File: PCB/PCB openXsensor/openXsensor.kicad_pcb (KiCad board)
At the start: 2 copper layers, 35.6 x 34.3 mm, 18 parts, among them P1 Digital, P10 VFAS/COURANT, P11 GY-86, P12 NTC1, P13 NTC2, P14 ISP1, P15 ISP2, P16 4S, P17 ADS1115, P2 Analog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

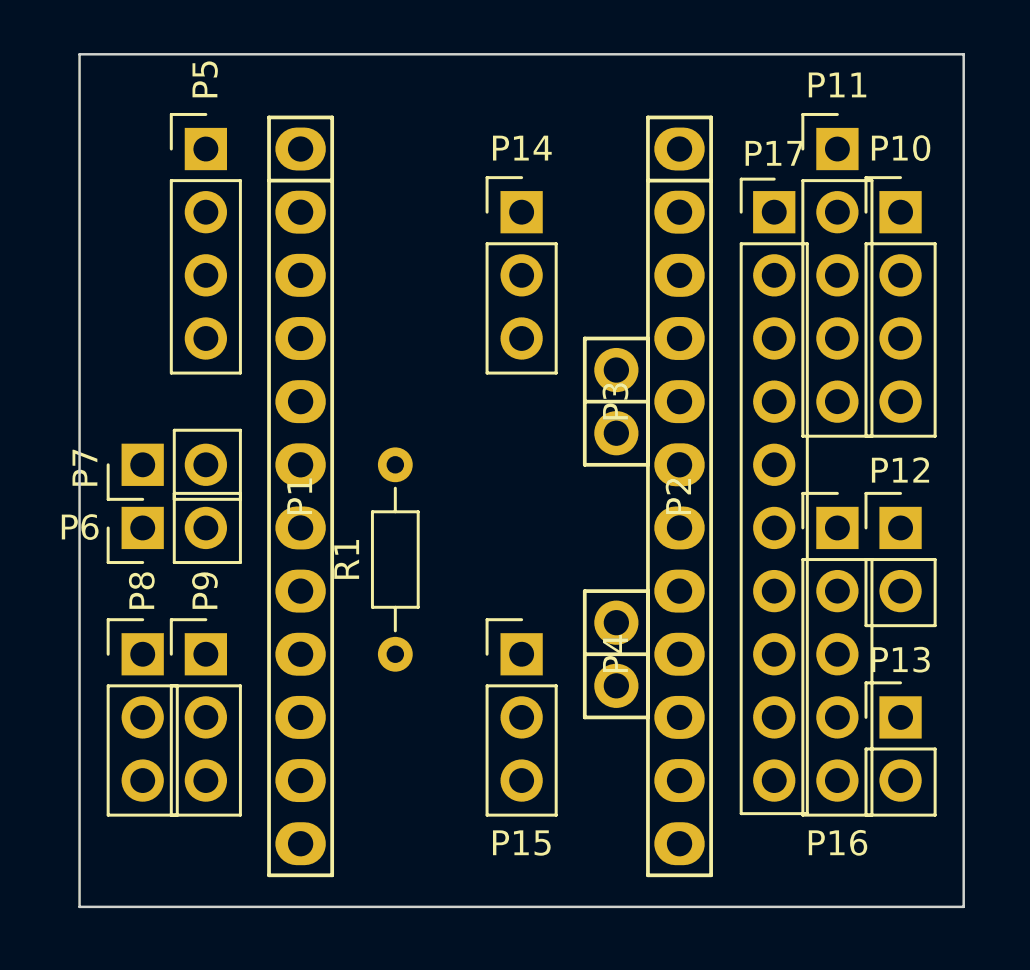
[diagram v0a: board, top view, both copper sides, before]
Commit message: Update oXs pcb proto
Add protection resistors for 4s ans sport/hub connectors.
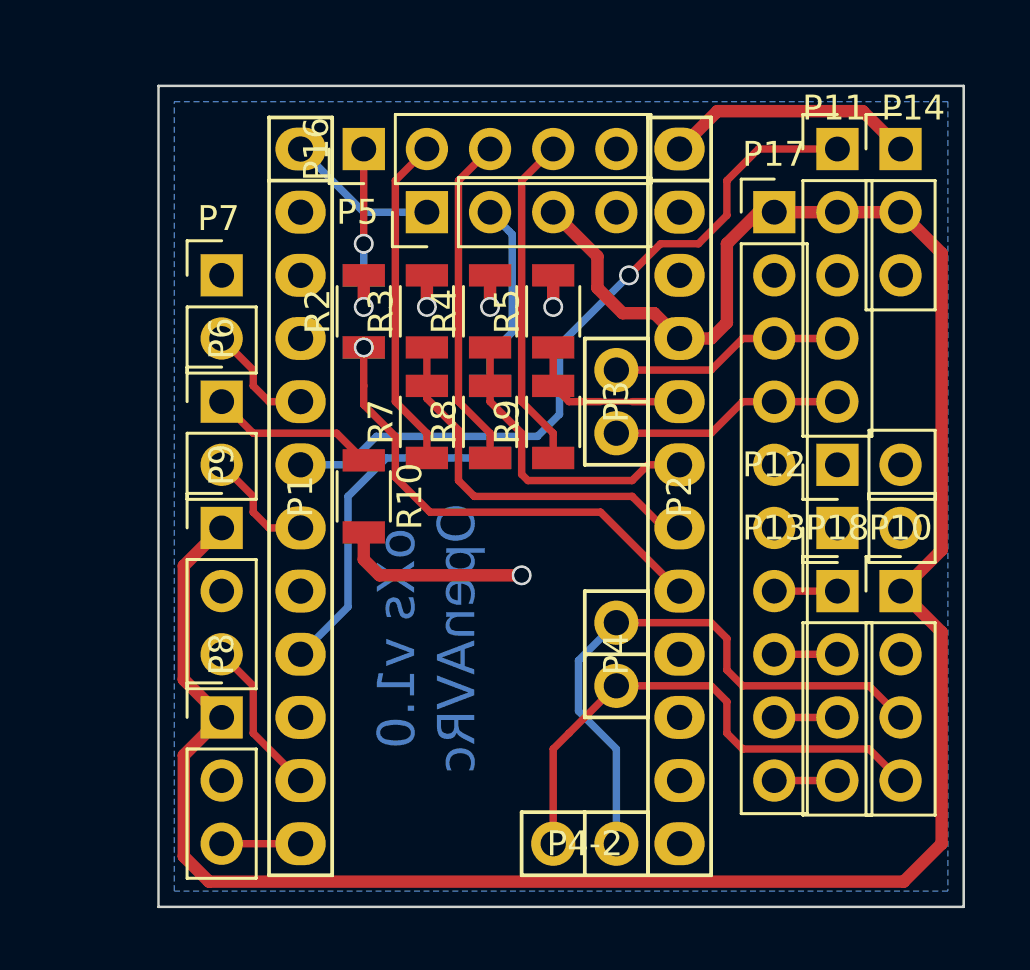
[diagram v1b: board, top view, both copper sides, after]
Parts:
- removed P15: ISP2, Pin_Header_Straight_1x03_Pitch2.54mm
- added P18: ADS_IN, Pin_Header_Straight_1x04_Pitch2.54mm, F.Cu at (160.0, 102.9)
- added P4-2: ADC, Socket_Arduino_Pro_Mini:Socket_Strip_Arduino_1x02, F.Cu at (151.1, 113.0)
- added R10: 220, R_1206, F.Cu at (141.0, 99.1)
- added R2: 20K, R_1206, F.Cu at (141.0, 91.6)
- added R3: 20K, R_1206, F.Cu at (143.5, 91.6)
- added R4: 20K, R_1206, F.Cu at (146.1, 91.6)
- added R5: 20K, R_1206, F.Cu at (148.6, 91.6)
- added R6: 51K, R_1206, B.Cu at (141.0, 91.6)
- added R7: 51K, R_1206, F.Cu at (143.5, 96.1)
- added R8: 51K, R_1206, F.Cu at (146.1, 96.1)
- added R9: 51K, R_1206, F.Cu at (148.6, 96.1)
- P14: value ISP1 -> ALIM
- R1: footprint R_Axial_DIN0204_L3.6mm_D1.6mm_P7.62mm_Horizontal -> R_1206; moved to B.Cu
- moved P16 24.4 mm to (141.0, 85.1), turned to 90 degrees
- moved P14 15.5 mm to (162.6, 85.1)
- moved P10 15.2 mm to (162.6, 102.9)
- moved R1 10.1 mm to (146.1, 96.1)
- moved P5 9.25 mm to (143.5, 87.6), turned to 90 degrees
- moved P7 8.25 mm to (135.3, 90.2), turned to 0 degrees
- moved P13 8.03 mm to (160.0, 100.3), turned to 90 degrees
- moved P6 5.99 mm to (135.3, 95.2), turned to 0 degrees
- moved P9 5.12 mm to (135.3, 100.3)
- moved P8 4.07 mm to (135.3, 108.0)
- moved P12 3.59 mm to (160.0, 97.8), turned to 90 degrees
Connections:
- P10 pad 3: /A0 -> /A7
- P10 pad 4: /A1 -> /A6
- P14 pad 1: GND -> /RAW
- P14 pad 2: /Reset -> VCC
- P14 pad 3: VCC -> GND
- P16 pad 1: /A2 -> Net-(P16-Pad1)
- P16 pad 2: /A3 -> Net-(P16-Pad2)
- P16 pad 3: /A6 -> Net-(P16-Pad3)
- P16 pad 4: /A7 -> Net-(P16-Pad4)
- P16 pad 5: GND -> (no net)
- P17 pad 10: (no net) -> Net-(P17-Pad10)
- P17 pad 7: (no net) -> Net-(P17-Pad7)
- P17 pad 8: (no net) -> Net-(P17-Pad8)
- P17 pad 9: (no net) -> Net-(P17-Pad9)
- P2 pad 1: (no net) -> /RAW
- P2 pad 10: /12(MISO) -> (no net)
- P2 pad 11: /11(**/MOSI) -> (no net)
- P2 pad 3: /Reset -> (no net)
- P2 pad 9: /13(SCK) -> (no net)
- P6 pad 1: GND -> Net-(P6-Pad1)
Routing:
- net VCC: track 0.00 -> 94.9 mm
- net /3(**): track 0.00 -> 29.3 mm, vias 0 -> 1
- net /A7: track 0.00 -> 23.9 mm
- net /A6: track 0.00 -> 21.2 mm
- net /A0: track 0.00 -> 19.1 mm, vias 0 -> 1
- net /A1: track 0.00 -> 15.6 mm
- net /6(**): track 0.00 -> 13.5 mm
- net Net-(P16-Pad4): track 0.00 -> 13.5 mm
- net Net-(P16-Pad3): track 0.00 -> 13.5 mm
- net Net-(P16-Pad2): track 0.00 -> 13.5 mm
- net GND: track 0.00 -> 12.8 mm, vias 0 -> 5
- net /A2: track 0.00 -> 12.3 mm
- net /RAW: track 0.00 -> 10.2 mm
- net /A5: track 0.00 -> 9.42 mm
- net /A4: track 0.00 -> 9.42 mm
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- added copper zone on B.Cu, net GND
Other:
- board size 35.6 x 34.3 mm -> 32.4 x 33 mm
- net class ALIM added: clearance 0.25, trace_width 0.5, via_dia 0.8, via_drill 0.6
- net class Default: clearance 0.2 -> 0.25; trace_width 0.25 -> 0.3; via_dia 0.6 -> 0.8; via_drill 0.4 -> 0.6
- rule trace_clearance: 0.2 -> 0.25
- rule via_min_drill: 0.3 -> 0.6
- rule via_min_size: 0.4 -> 0.8
- board text added: "oXs v1.0 OpenAVRc"

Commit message: Update oXs pcb
Add resistors protection on Vfas et current
Add 5v pin on Sport connector
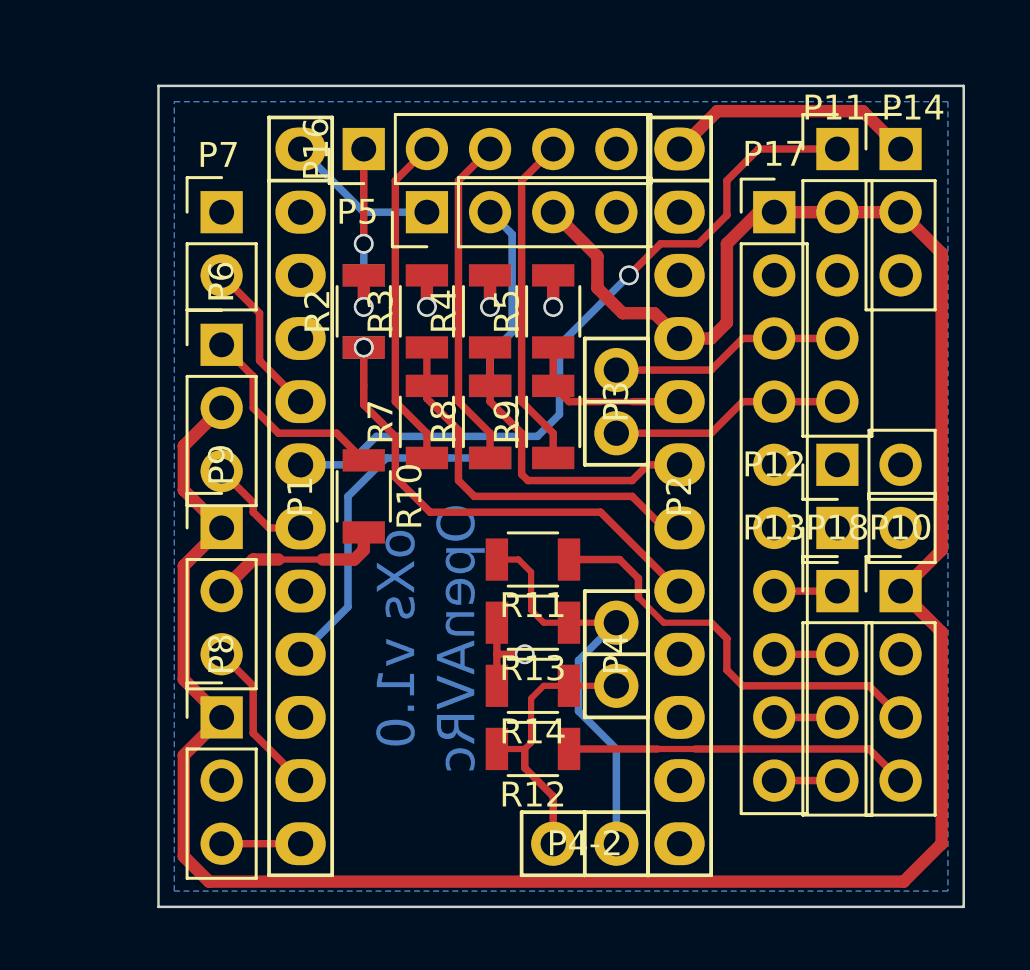
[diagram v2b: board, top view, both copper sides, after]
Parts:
- added R11: 51K, R_1206, F.Cu at (147.8, 101.6)
- added R12: 51K, R_1206, F.Cu at (147.8, 109.2)
- added R13: 20K, R_1206, F.Cu at (147.8, 104.1)
- added R14: 20K, R_1206, F.Cu at (147.8, 106.7)
- P6: footprint Pin_Header_Straight_1x02_Pitch2.54mm -> Pin_Header_Straight_1x03_Pitch2.54mm
- moved P7 2.54 mm to (135.3, 87.6)
- moved P6 2.29 mm to (135.3, 93.0)
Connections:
- P10 pad 3: /A7 -> Net-(P10-Pad3)
- P10 pad 4: /A6 -> Net-(P10-Pad4)
- P6 pad 2: /4 -> VCC
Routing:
- net Net-(P10-Pad3): track 0.00 -> 17.2 mm
- net Net-(P10-Pad4): track 0.00 -> 13.9 mm
- net /A6: track 21.2 -> 11.2 mm
- net /A7: track 23.9 -> 16.9 mm
- net VCC: track 94.9 -> 101.0 mm
- net GND: track 12.8 -> 15.8 mm
- net /2: track 4.60 -> 6.40 mm
- net Net-(P6-Pad1): track 6.69 -> 8.38 mm

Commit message: Update oXs pcb
Move connectors p8 p9 under pro mini
Add connector between 5v and sport connector. 
Add gnd ads1115 addr pin (0x48).
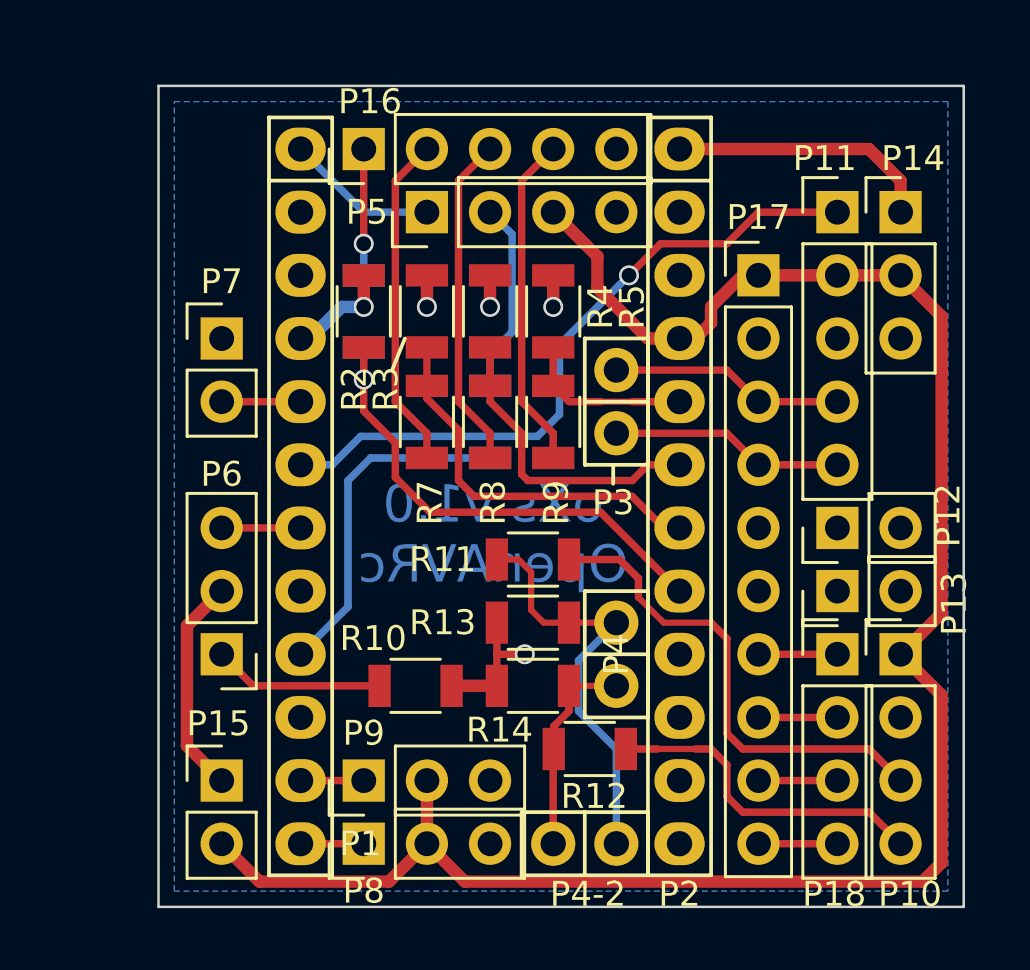
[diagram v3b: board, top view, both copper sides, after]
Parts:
- added P15: STRAP, Pin_Header_Straight_1x02_Pitch2.54mm, F.Cu at (135.3, 110.5)
- moved P6 12.4 mm to (135.3, 105.4), turned to 180 degrees
- moved P9 11.7 mm to (141.0, 110.5), turned to 90 degrees
- moved R10 7.90 mm to (143.1, 106.7), turned to 0 degrees
- moved P8 7.65 mm to (141.0, 113.0), turned to 90 degrees
- moved P7 5.08 mm to (135.3, 92.7)
- moved P17 2.62 mm to (156.8, 90.2)
- moved P13 2.54 mm to (160.0, 102.9)
- moved P10 2.54 mm to (162.6, 105.4)
- moved P11 2.54 mm to (160.0, 87.6)
- moved P12 2.54 mm to (160.0, 100.3)
- moved P14 2.54 mm to (162.6, 87.6)
- moved P18 2.54 mm to (160.0, 105.4)
- moved R12 2.29 mm to (150.1, 109.2)
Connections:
- P17 pad 5: (no net) -> GND
- P6 pad 2: VCC -> Net-(P15-Pad1)
- P8 pad 1: VCC -> /9(**)
- P8 pad 2: GND -> VCC
- P8 pad 3: /9(**) -> GND
- P9 pad 1: VCC -> /8
- P9 pad 2: GND -> VCC
- P9 pad 3: /8 -> GND
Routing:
- net VCC: track 101.0 -> 77.6 mm
- net Net-(P15-Pad1): track 0.00 -> 8.78 mm
- net /8: track 6.40 -> 2.54 mm
- net /2: track 6.40 -> 3.18 mm
- net /A6: track 11.2 -> 8.52 mm
- net Net-(P10-Pad3): track 17.2 -> 19.7 mm
- net GND: track 15.8 -> 13.6 mm
- net /3(**): track 29.3 -> 27.4 mm
- net Net-(P6-Pad1): track 8.38 -> 6.88 mm
- net /A0: track 19.1 -> 20.4 mm
- net /4: track 4.35 -> 3.18 mm
- net /9(**): track 3.18 -> 2.54 mm
- net Net-(P17-Pad9): track 2.54 -> 3.18 mm
- net Net-(P17-Pad7): track 2.54 -> 3.18 mm
- net Net-(P17-Pad10): track 2.54 -> 3.18 mm
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
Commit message: Update pcb oxs
Change wire on gps connector
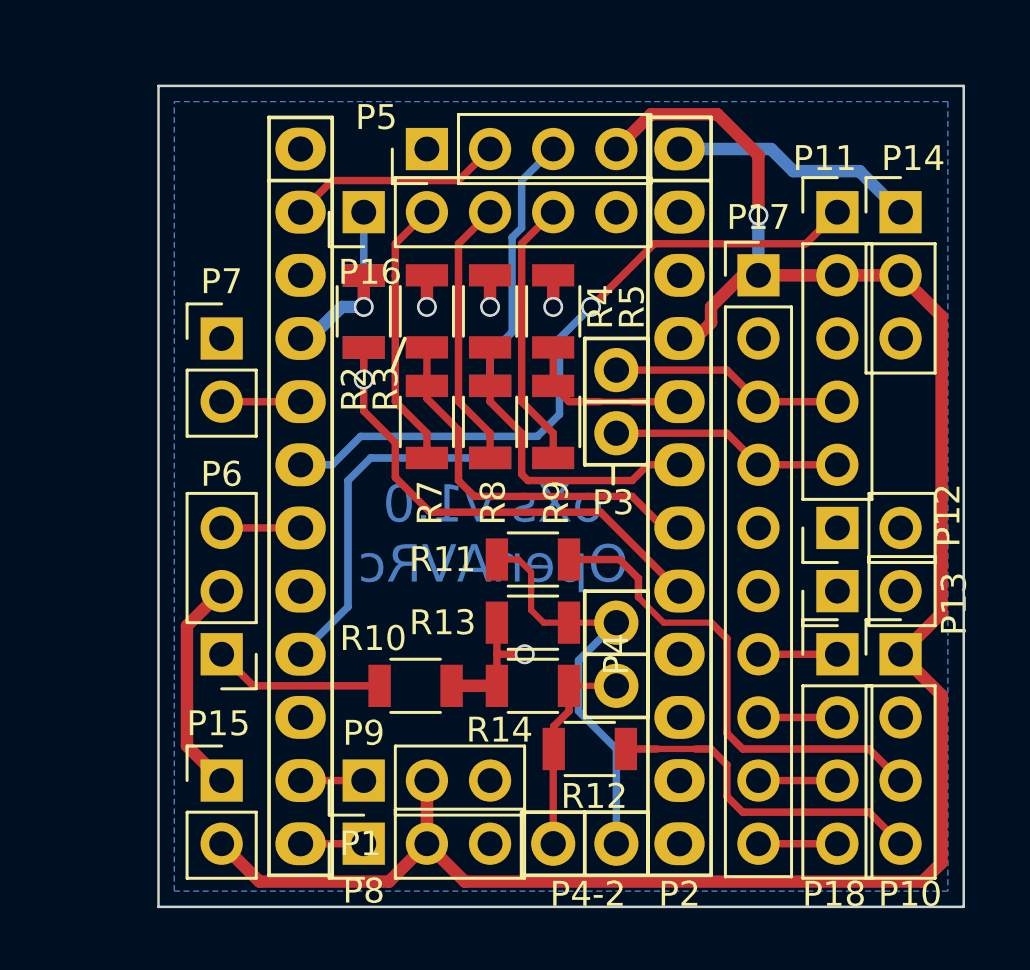
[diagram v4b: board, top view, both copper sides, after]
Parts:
- moved P16 2.54 mm to (141.0, 87.6)
- moved P5 2.54 mm to (143.5, 85.1)
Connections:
- P1 pad 1: /1(Tx) -> (no net)
- P1 pad 2: (no net) -> /0(Rx)
- P5 pad 1: /1(Tx) -> GND
- P5 pad 2: Net-(P5-Pad2) -> /0(Rx)
- P5 pad 3: VCC -> Net-(P5-Pad3)
- P5 pad 4: GND -> VCC
- R1 pad 2: Net-(P5-Pad2) -> Net-(P5-Pad3)
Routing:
- net Net-(P5-Pad3): track 0.00 -> 10.6 mm
- net /0(Rx): track 0.00 -> 8.67 mm
- net Net-(P5-Pad2): track 7.72 -> 0.00 mm
- net /1(Tx): track 6.13 -> 0.00 mm
- net VCC: track 77.6 -> 81.5 mm, vias 0 -> 1
- net Net-(P16-Pad1): track 5.33 -> 2.54 mm, vias 1 -> 0
- net Net-(P16-Pad2): track 13.5 -> 10.9 mm
- net Net-(P16-Pad4): track 13.5 -> 10.9 mm
- net Net-(P16-Pad3): track 13.5 -> 10.9 mm
- net /RAW: track 10.7 -> 9.94 mm

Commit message: Update oXs pcb
Add sequencer connector
Add capacitors on analog input 
Add capacitors on 5v and raw power 
...
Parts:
- removed P4-2: ADC, Socket_Arduino_Pro_Mini:Socket_Strip_Arduino_1x02
- removed R12: 51K, R_1206
- removed R13, R14: 20K, R_1206
- added C1: 100nF, Empreintes:C_1206, B.Cu at (147.7, 103.5)
- added C10: 100nF, Empreintes:C_1206, F.Cu at (147.7, 106.7)
- added C11: 100nF, Empreintes:C_1206, F.Cu at (147.7, 104.1)
- added C14: 100nF, Empreintes:C_1206, B.Cu at (143.8, 108.0)
- added C2: 100nF, Empreintes:C_1206, B.Cu at (147.7, 101.0)
- added C3: 100nF, Empreintes:C_1206, B.Cu at (147.7, 98.4)
- added C4: 100nF, Empreintes:C_1206, B.Cu at (147.7, 95.9)
- added C5: 10uF, Empreintes:CP_EIA-3216-18_Kemet-A_Pad1.58x1.35mm_HandSolder, B.Cu at (157.5, 85.9)
- added C6: 10uF, Empreintes:CP_EIA-3216-18_Kemet-A_Pad1.58x1.35mm_HandSolder, F.Cu at (158.6, 85.1)
- added C7: 100nF, Empreintes:C_1206, B.Cu at (160.9, 113.0)
- added C8: 100nF, Empreintes:C_1206, F.Cu at (160.0, 102.0)
- added C9: 100nF, Empreintes:C_1206, F.Cu at (160.9, 113.0)
- added P19: MPXV7002DP, Pin_Header_Straight_1x03_Pitch2.54mm, F.Cu at (160.0, 105.4)
- P12, P13, P16, P5, P8, P9: moved to B.Cu
- P15: value STRAP -> SEQUENCEUR; footprint Pin_Header_Straight_1x02_Pitch2.54mm -> Pin_Header_Straight_1x04_Pitch2.54mm
- P18: value ADS_IN -> MS4525DO
- R11: value 51K -> 0
- moved P12 17.1 mm to (148.6, 113.0), turned to 0 degrees
- moved P13 13.5 mm to (151.1, 113.0), turned to 0 degrees
- moved P18 13.0 mm to (162.6, 92.7)
- moved R10 8.07 mm to (141.0, 98.9), turned to 270 degrees
- moved P6 7.62 mm to (135.3, 97.8), turned to 0 degrees
- moved R11 6.99 mm to (141.9, 105.4), turned to 0 degrees
- moved P15 5.08 mm to (135.3, 105.4)
- moved R1 2.69 mm to (144.1, 94.2)
- moved P10 2.54 mm to (162.6, 102.9)
- moved P14 2.54 mm to (162.6, 85.1)
- moved P7 2.54 mm to (135.3, 90.2)
- turned P16 to 270 degrees
- turned P5 to 270 degrees
- turned P8 to 270 degrees
- turned P9 to 270 degrees
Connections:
- P1 pad 12: /9(**) -> /SEQ1
- P10 pad 3: Net-(P10-Pad3) -> /ADS_VOLT1
- P10 pad 4: Net-(P10-Pad4) -> /ADS_VOLT2
- P12 pad 1: (no net) -> /A6
- P13 pad 1: (no net) -> /A7
- P15 pad 1: Net-(P15-Pad1) -> /SEQ4
- P15 pad 2: VCC -> /SEQ3
- P17 pad 10: Net-(P17-Pad10) -> /ADS_VOLT4
- P17 pad 7: Net-(P17-Pad7) -> /ADS_VOLT1
- P17 pad 8: Net-(P17-Pad8) -> /ADS_VOLT2
- P17 pad 9: Net-(P17-Pad9) -> /ADS_VOLT3
- P18 pad 1: Net-(P17-Pad7) -> VCC
- P18 pad 2: Net-(P17-Pad8) -> /A5
- P18 pad 3: Net-(P17-Pad9) -> /A4
- P18 pad 4: Net-(P17-Pad10) -> GND
- P2 pad 10: (no net) -> /SEQ4
- P2 pad 11: (no net) -> /SEQ3
- P2 pad 12: (no net) -> /SEQ2
- P6 pad 2: Net-(P15-Pad1) -> Net-(P6-Pad2)
- P8 pad 1: /9(**) -> /ADS_VOLT4
- R11 pad 1: Net-(P10-Pad3) -> Net-(P6-Pad2)
- R11 pad 2: /A7 -> VCC
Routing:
- net /SEQ2: track 0.00 -> 25.9 mm, vias 0 -> 2
- net /ADS_VOLT4: track 0.00 -> 22.6 mm
- net Net-(P10-Pad3): track 19.7 -> 0.00 mm
- net /SEQ4: track 0.00 -> 19.6 mm
- net /SEQ3: track 0.00 -> 19.5 mm
- net Net-(P6-Pad2): track 0.00 -> 15.0 mm
- net Net-(P10-Pad4): track 13.4 -> 0.00 mm
- net /ADS_VOLT1: track 0.00 -> 10.7 mm
- net /ADS_VOLT2: track 0.00 -> 10.7 mm
- net VCC: track 81.5 -> 90.4 mm, vias 1 -> 2
- net Net-(P15-Pad1): track 8.78 -> 0.00 mm
- net GND: track 13.6 -> 21.6 mm, vias 5 -> 10
- net /ADS_VOLT3: track 0.00 -> 6.77 mm
- net /A0: track 20.4 -> 25.6 mm
- net /A7: track 16.9 -> 12.0 mm
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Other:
- board text added: "OpenAVRc oXs v1.0"
- board text removed: "oXs v1.0 OpenAVRc"
